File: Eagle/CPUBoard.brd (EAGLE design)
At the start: 100 x 80 mm, 29 parts, among them IC2 MAX232, IC3 MAX485CPA, Q1 12.000MHz, X2 RELAY_BOARD, X4 DISPLAY, X6 MKDSN1,5/3-5,08, X7 MKDSN1,5/3-5,08, X8 BUTTON_BOARD

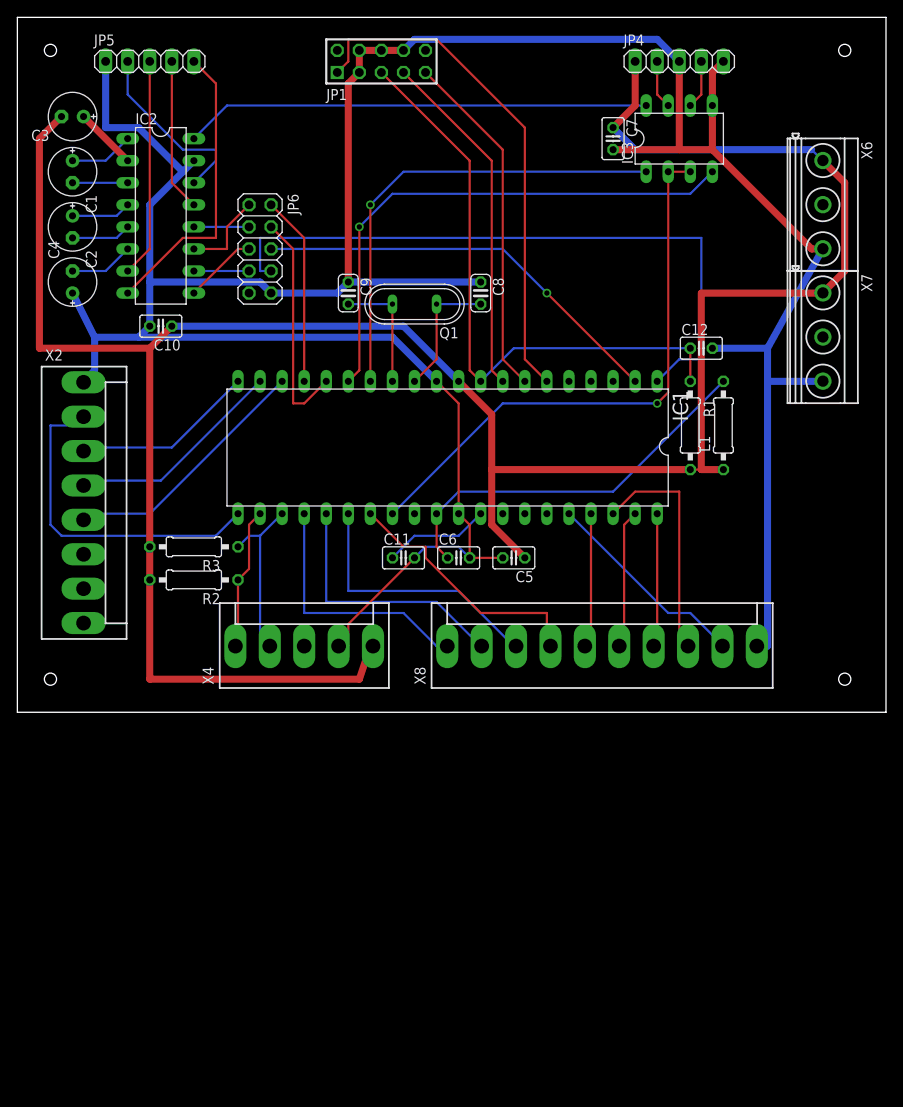
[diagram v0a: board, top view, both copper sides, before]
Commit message: - corrections for CPUBoard:   - RS-485 need termination resistors etc.   - connectors are wrong, use 22-?-05 tec. from con-molex -> connectors on other boards must be replaced, too!
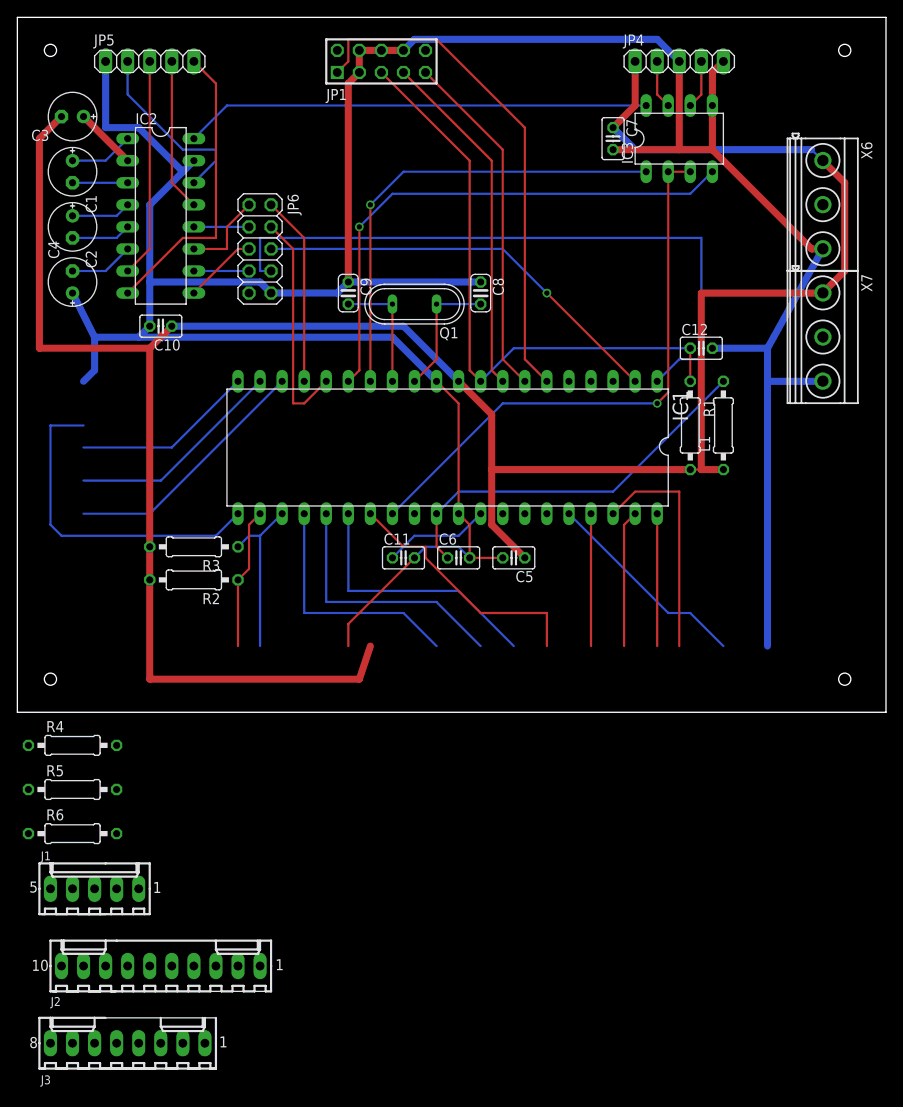
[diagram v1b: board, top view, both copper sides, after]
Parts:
- removed X2: RELAY_BOARD, con-molex:KK-156-8
- removed X4: DISPLAY, con-molex:KK-156-5
- removed X8: BUTTON_BOARD, con-molex:KK-156-10
- added J1: DISPLAY, con-molex:6410-05
- added J2: BUTTON_BOARD, con-molex:6410-10
- added J3: RELAY_BOARD, con-molex:6410-08
- added R4: 120, rcl:0207/10
- added R5, R6: 1k, rcl:0207/10
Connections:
- net +5V: now also J1.5, R5.2; no longer X4.5
- net GND: now also J1.4, J2.10, J3.1, R6.1; no longer X2.1, X4.4, X8.10
- net LED_GREEN: now also J2.1; no longer X8.1
- net LED_L: now also J2.3; no longer X8.3
- net LED_R: now also J2.4; no longer X8.4
- net LED_YELLOW: now also J2.2; no longer X8.2
- net LEFT: now also J2.6; no longer X8.6
- net N$17: now also R4.1, R6.2
- net N$18: now also R4.2, R5.1
- net PRESET_LEFT: now also J2.5; no longer X8.5
- net PRESET_RIGHT: now also J2.9; no longer X8.9
- net REL1: now also J3.2; no longer X2.2
- net REL2: now also J3.3; no longer X2.3
- net REL3: now also J3.4; no longer X2.4
- net REL4: now also J3.5; no longer X2.5
- net RIGHT: now also J2.8; no longer X8.8
- net SCL: now also J1.1; no longer X4.1
- net SDA: now also J1.2; no longer X4.2
- net SPARE: now also J1.3; no longer X4.3
- net STOP: now also J2.7; no longer X8.7
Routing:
- net GND: track 357.8 -> 355.4 mm
- net LED_GREEN: track 29.5 -> 28.2 mm
- net SDA: track 20.5 -> 19.4 mm
- net REL1: track 39.4 -> 38.4 mm
- net RIGHT: track 27.5 -> 26.5 mm
- net PRESET_LEFT: track 16.0 -> 15.2 mm
- net REL4: track 29.9 -> 29.2 mm
- net REL3: track 25.6 -> 25.1 mm
- net LEFT: track 16.3 -> 15.8 mm

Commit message: - corrections for RelayBoard1:   - using right connectors from library con-molex   - single sided routing - corrections for ButtonBoard:   - using right connector from library con-molex   - using right switches from library switch-misc (SRK/SRKL) - component placement & board layout for ButtonBoard done - CPUBoard:   - some components moved around the board   - re-routing (partially)
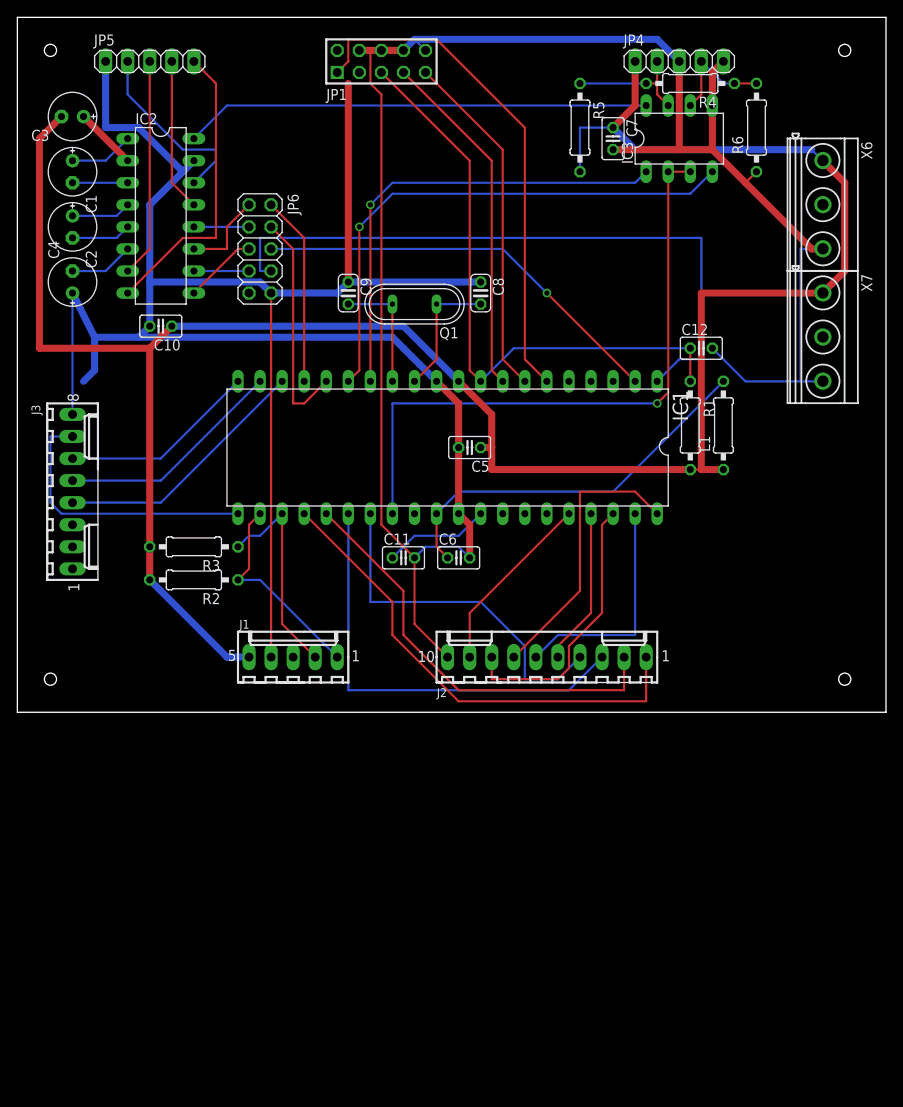
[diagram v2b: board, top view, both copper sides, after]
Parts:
- moved R6 113.2 mm to (85.1, 67.3), turned to 90 degrees
- moved R4 104.2 mm to (77.5, 72.4), turned to 180 degrees
- moved R5 96.0 mm to (64.8, 67.3), turned to 270 degrees
- moved J3 63.8 mm to (6.35, 25.4), turned to 270 degrees
- moved J2 56.9 mm to (61.0, 6.35)
- moved J1 35.1 mm to (31.8, 6.35)
- moved C5 13.7 mm to (52.1, 30.5)
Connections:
- net GND: now also J3.8, JP1.10; no longer J3.1, JP1.3
- net REL1: now also J3.7; no longer J3.2
- net REL2: now also J3.6; no longer J3.3
- net REL3: now also J3.5; no longer J3.4
- net REL4: now also J3.4; no longer J3.5
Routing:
- net GND: track 355.4 -> 438.9 mm
- net LED_GREEN: track 28.2 -> 55.6 mm
- net +5V: track 282.2 -> 256.1 mm
- net LED_L: track 30.6 -> 51.1 mm
- net LED_YELLOW: track 30.0 -> 49.5 mm
- net STOP: track 15.2 -> 32.1 mm
- net LED_R: track 29.6 -> 41.3 mm
- net LEFT: track 15.8 -> 26.5 mm
- net N$18: track 5.61 -> 14.5 mm
- net SCL: track 16.3 -> 23.8 mm
- net N$15: track 65.5 -> 72.9 mm
- net N$17: track 5.61 -> 13.0 mm
- net REL1: track 38.4 -> 32.3 mm
- net SDA: track 19.4 -> 24.7 mm
- net RIGHT: track 26.5 -> 31.8 mm
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
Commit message: - CPUBoard:   - another pin-header added for RS-485 UART   - correct termination for RS-485 A/B lines - PowerSupply: terminals added - eagle_clean.sh: remove backup files of Eagle
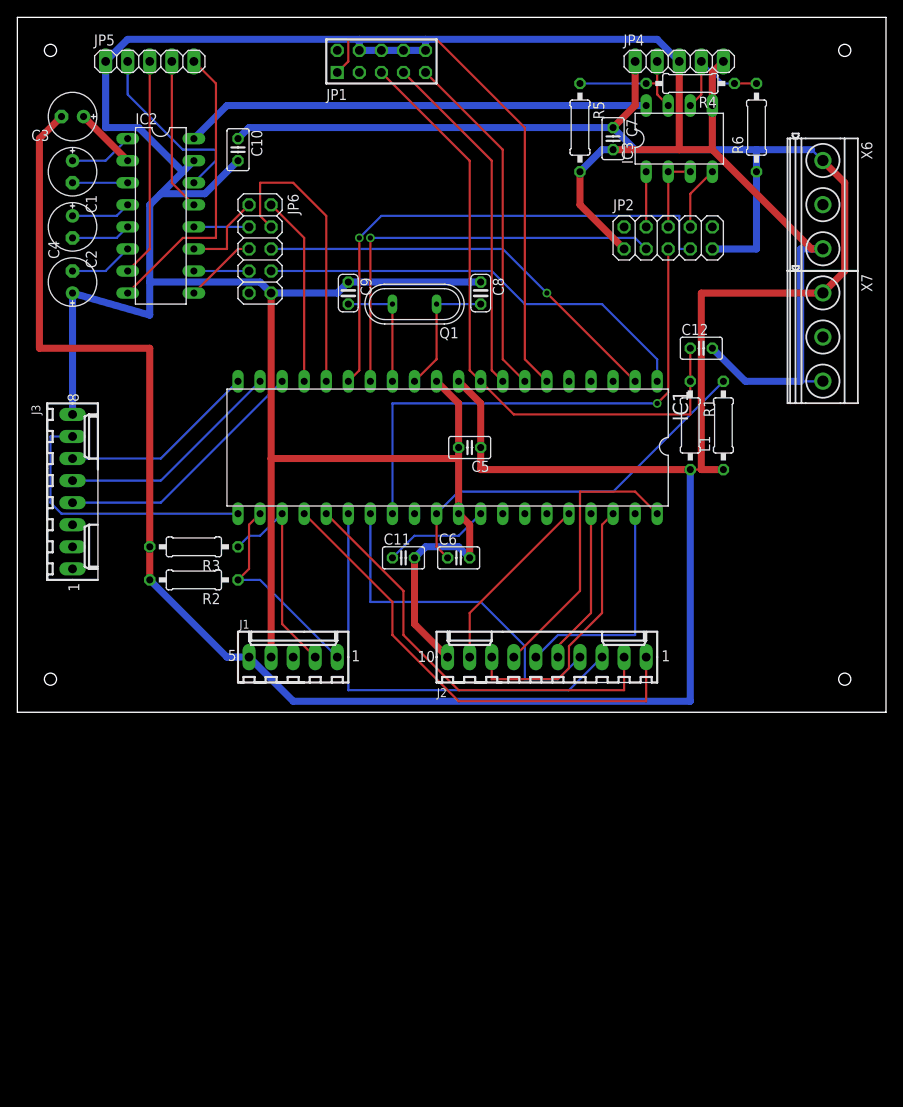
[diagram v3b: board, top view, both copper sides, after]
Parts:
- added JP2: (no value), pinhead:2X05
- moved C10 22.2 mm to (25.4, 64.8), turned to 270 degrees
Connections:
- new net N$20: IC3.2, IC3.3, JP2.6
- new net N$21: IC3.4, JP2.8
- new net N$23: IC3.1, JP2.4
- net +5V: now also JP2.9, R6.1; no longer R5.2
- net GND: now also JP2.1, R5.2; no longer R6.1
- net N$13: now also JP2.3; no longer IC3.1
- net N$14: now also JP2.7; no longer IC3.4
- net N$15: now also JP2.5; no longer IC3.2, IC3.3
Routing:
- net +5V: track 256.1 -> 347.3 mm
- net GND: track 438.9 -> 393.2 mm
- net N$31: track 76.0 -> 51.2 mm
- net N$15: track 72.9 -> 61.5 mm
- net N$20: track 0.00 -> 8.89 mm
- net N$16: track 26.2 -> 33.9 mm
- net N$21: track 0.00 -> 7.40 mm
- net N$23: track 0.00 -> 6.35 mm
- net N$13: track 53.6 -> 48.8 mm
- net N$3: track 69.8 -> 73.6 mm
- net N$14: track 61.6 -> 60.0 mm

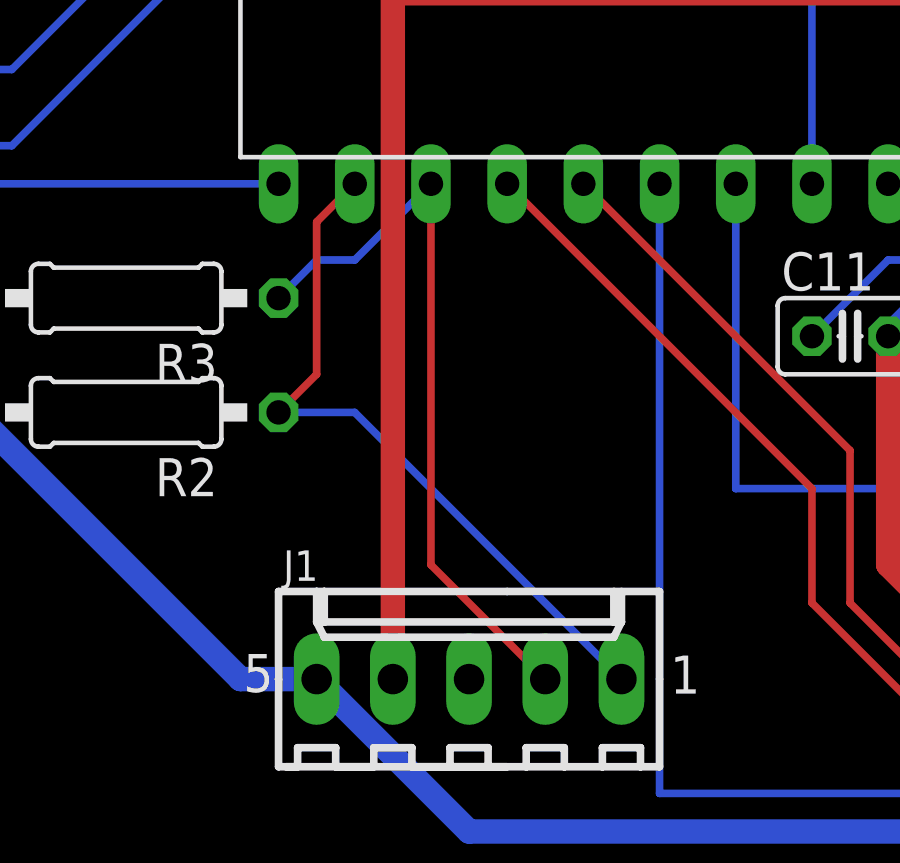
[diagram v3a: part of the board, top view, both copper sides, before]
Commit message: - CPUBoard: fix connections to display, somehow mirrored
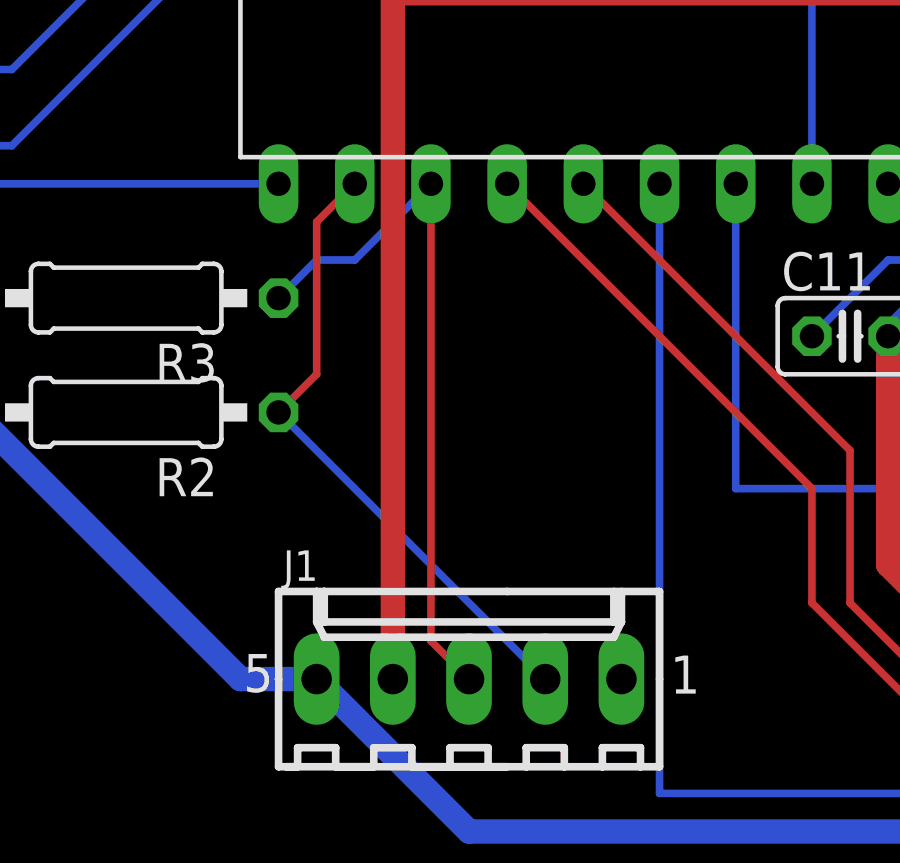
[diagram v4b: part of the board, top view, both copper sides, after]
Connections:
- removed net SPARE: J1.3
- new net DIO: J1.1
- net SCL: now also J1.2; no longer J1.1
- net SDA: now also J1.3; no longer J1.2
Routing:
- net SCL: track 23.8 -> 21.2 mm
- net SDA: track 24.7 -> 23.7 mm
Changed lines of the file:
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@@
 <wire x1="26.67" y1="16.51" x2="26.67" y2="21.59" width="0.254" layer="1"/>
 <wire x1="25.4" y1="15.24" x2="26.67" y2="16.51" width="0.254" layer="1"/>
-<contactref element="J1" pad="1"/>
-<wire x1="27.94" y1="15.24" x2="36.83" y2="6.35" width="0.254" layer="16"/>
-<wire x1="25.4" y1="15.24" x2="27.94" y2="15.24" width="0.254" layer="16"/>
+<contactref element="J1" pad="2"/>
+<wire x1="25.4" y1="15.24" x2="34.29" y2="6.35" width="0.254" layer="16"/>
 </signal>
 <signal name="SDA">
 <contactref element="IC1" pad="23"/>
 <contactref element="R3" pad="1"/>
-<contactref element="J1" pad="2"/>
 <wire x1="26.67" y1="20.32" x2="25.4" y2="19.05" width="0.254" layer="16"/>
 <wire x1="27.94" y1="20.32" x2="26.67" y2="20.32" width="0.254" layer="16"/>
 <wire x1="30.48" y1="22.86" x2="27.94" y2="20.32" width="0.254" layer="16"/>
-<wire x1="30.48" y1="10.16" x2="34.29" y2="6.35" width="0.254" layer="1"/>
-<wire x1="30.48" y1="22.86" x2="30.48" y2="10.16" width="0.254" layer="1"/>
+<contactref element="J1" pad="3"/>
+<wire x1="30.48" y1="7.62" x2="31.75" y2="6.35" width="0.254" layer="1"/>
+<wire x1="30.48" y1="22.86" x2="30.48" y2="7.62" width="0.254" layer="1"/>
 </signal>
 <signal name="N$12">
@@
 <wire x1="53.34" y1="22.86" x2="50.8" y2="20.32" width="0.254" layer="16"/>
 </signal>
-<signal name="SPARE">
-<contactref element="J1" pad="3"/>
-</signal>
 <signal name="N$17">
 <contactref element="IC3" pad="6"/>
@@
 <wire x1="77.47" y1="55.88" x2="77.47" y2="59.69" width="0.254" layer="1"/>
 </signal>
+<signal name="DIO">
+<contactref element="J1" pad="1"/>
+</signal>
 </signals>
